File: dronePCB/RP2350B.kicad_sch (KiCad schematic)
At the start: 43 parts, among them J1 BM03B-SRSS-TB, J2 USB_C_Receptacle, SW1 SW_BOOT, SW2 SW_RESET, U1 RP2350_80QFN, U2 W25Q128JVPIQ, U3 APS6404L-3SQR-ZR, Y1 ABM8-272-T3

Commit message: Started filling the BoM and changed some components
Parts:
- C10, C11, C12, C13, C14, C15, C17, C18, C4, C5, C6, C7, C8, C9: Link (none) -> https://www.mouser.pl/ProductDetail/KYOCERA-AVX/08056D104KA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; Manufacturer_Part_Number (none) -> 08056D104KAT2A; Price per unit (none) -> 0.031
- C19: Link (none) -> https://www.mouser.pl/ProductDetail/Samsung-Electro-Mechani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; Manufacturer_Part_Number (none) -> CL21B225KPFNNNE; Price per unit (none) -> 0.11
- C20, C21: Link (none) -> https://www.mouser.pl/ProductDetail/KEMET/C0805C150K1HACTU?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; Manufacturer_Part_Number (none) -> C0805C150K1HACTU; Price per unit (none) -> 0.10
- D1: value NSR0530HT1G -> ARB551V-30-HF; Link (none) -> https://www.mouser.pl/ProductDetail/Comchip-Technology/ARB5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; Manufacturer_Part_Number (none) -> ARB551V-30-HF; Price per unit (none) -> 0.411

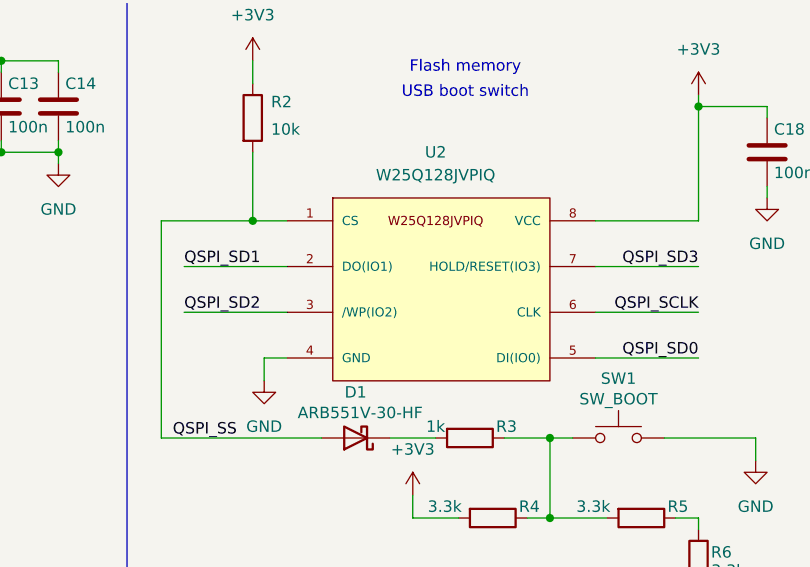
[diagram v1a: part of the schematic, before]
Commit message: Added more information to BoM
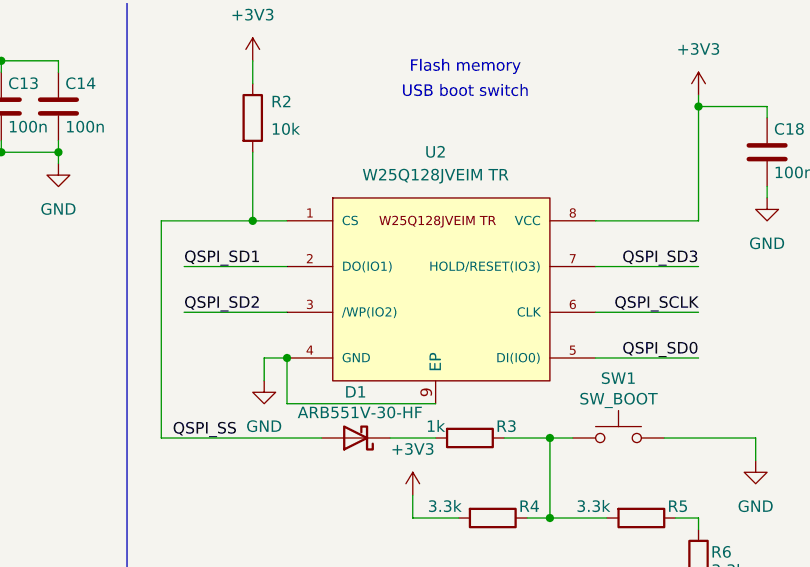
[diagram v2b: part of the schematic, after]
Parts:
- J1: Link (none) -> https://www.tme.eu/pl/details/bm03b-srss-tb/zlacza-sygnalow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; Manufacturer_Part_Number (none) -> BM03B-SRSS-TB; Price per unit (none) -> 0.484
- J2: Link (none) -> https://www.mouser.pl/ProductDetail/Amphenol-Commercial-Pro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; Manufacturer_Part_Number (none) -> 12401610E4#2A; Price per unit (none) -> 1.26
- L1: Link (none) -> https://www.mouser.pl/ProductDetail/ABRACON/AOTA-B201610S3R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; Manufacturer_Part_Number (none) -> AOTA-B201610S3R3-101-T; Price per unit (none) -> 0.211
- SW1, SW2: Link (none) -> https://www.mouser.pl/ProductDetail/Wurth-Elektronik/434133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; Manufacturer_Part_Number (none) -> 434133025816; Price per unit (none) -> 0.55
- U1: Link (none) -> https://www.mouser.pl/ProductDetail/Raspberry-Pi/SC151013-A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; Manufacturer_Part_Number (none) -> SC1510(13)-A4; Price per unit (none) -> 0.907
- U2: value W25Q128JVPIQ -> W25Q128JVEIM TR; footprint Flash:W25Q128JVPIQ -> droneParts:SON127P800X600X80-9N-D; Link (none) -> https://www.mouser.pl/ProductDetail/Winbond/W25Q128JVEIM-TR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; Manufacturer_Part_Number (none) -> W25Q128JVEIM TR; Price per unit None -> 2.38
- U3: Link (none) -> https://www.mouser.pl/ProductDetail/AP-Memory/APS6404L-3SQR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; Manufacturer_Part_Number (none) -> APS6404L-3SQR-ZR; Price per unit None -> 2.19
- Y1: Link (none) -> https://www.mouser.pl/ProductDetail/ABRACON/ABM8-272-T3?qs=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; Manufacturer_Part_Number (none) -> ABM8-272-T3; Price per unit (none) -> 0.54

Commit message: Finished the BoM
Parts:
- R1: Link (none) -> https://www.mouser.pl/ProductDetail/Vishay/CRCW080533R0JNEA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; Manufacturer_Part_Number (none) -> CRCW080533R0JNEA; Price per unit (none) -> 0.10
- R10, R9: Link (none) -> https://www.mouser.pl/ProductDetail/Vishay/CRCW080527R0FKEA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; Manufacturer_Part_Number (none) -> CRCW080527R0FKEA; Price per unit (none) -> 0.10
- R11, R12: Link (none) -> https://www.mouser.pl/ProductDetail/Susumu/RG2012P-472-B-T5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; Manufacturer_Part_Number (none) -> RG2012P-472-B-T5; Price per unit (none) -> 0.10
- R2: Link (none) -> https://www.mouser.pl/ProductDetail/Bourns/CRM0805-FX-1002E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; Manufacturer_Part_Number (none) -> CRM0805-FX-1002ELF; Price per unit (none) -> 0.041
- R3, R8: Link (none) -> https://www.mouser.pl/ProductDetail/Bourns/CRM0805-FX-1001E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; Manufacturer_Part_Number (none) -> CRM0805-FX-1001ELF; Price per unit (none) -> 0.10
- R4, R5, R6: Link (none) -> https://www.mouser.pl/ProductDetail/KOA-Speer/SG73S2ARTTD33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; Manufacturer_Part_Number (none) -> SG73S2ARTTD3301F; Price per unit (none) -> 0.222
- R7: Link (none) -> https://www.mouser.pl/ProductDetail/Bourns/CR0805AFX-1003EA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; Manufacturer_Part_Number (none) -> CR0805AFX-1003EAS; Price per unit (none) -> 0.10
